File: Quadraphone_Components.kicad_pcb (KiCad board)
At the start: 4 copper layers, 60 x 100 mm, 196 parts, among them J1 Conn_01x10_Male, J2 Conn_01x10_Male, J3 Conn_01x10_Male, J4 Conn_01x10_Male, J5 Eurorack_10_pin_power, Q1 MMBT3904, U1 AMS1117-5.0, U10 TL072, U11 74LV4066PW, U12 SSI2131, U13 TL072, U14 LM4040DBZ-2.5, U15 74LV4066PW, U16 TL072, U17 SSI2131, U18 TL072, U22 SSI2131, U3 MCP6002, U4 LM4040DBZ-5, U5 MCP6004, U6 74LV4066PW, U7 74LV4066PW, U8 74LV4066PW, U9 SSI2131

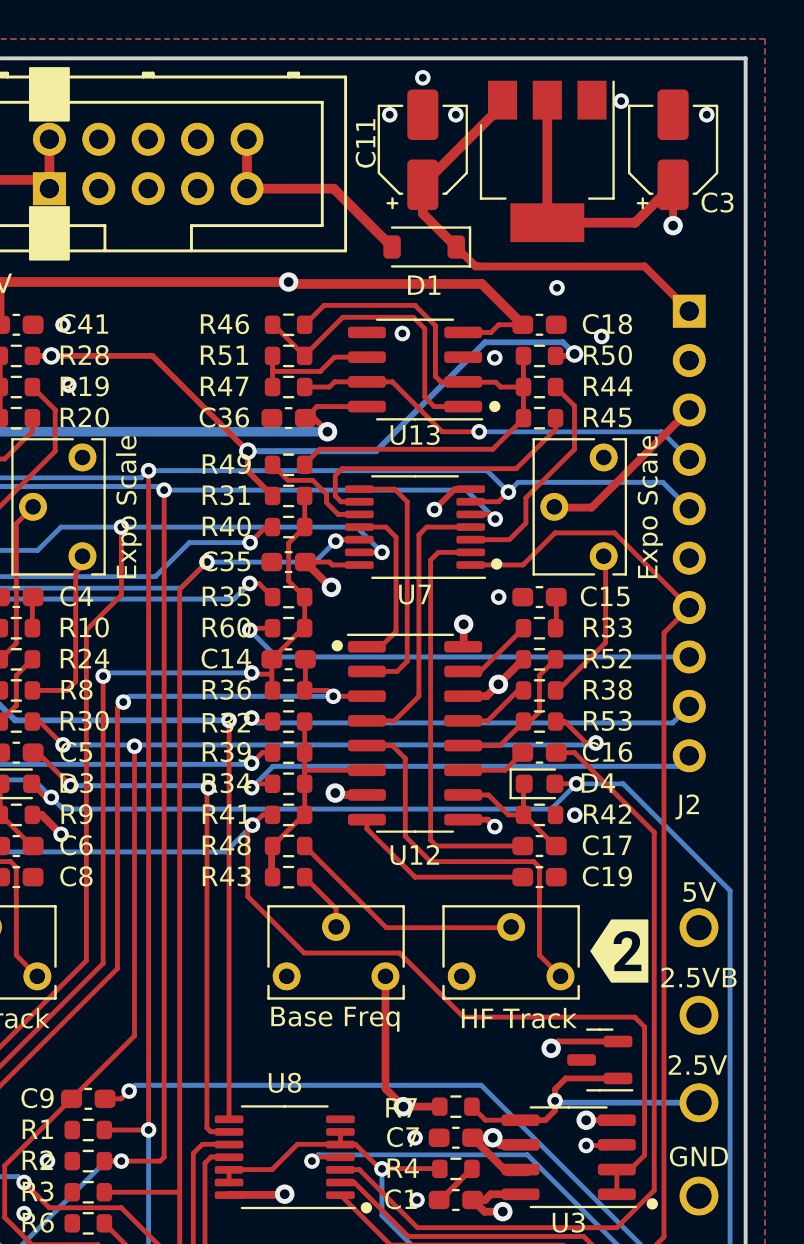
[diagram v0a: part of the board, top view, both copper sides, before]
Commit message: Updated resistor values in VCO tuning circuits
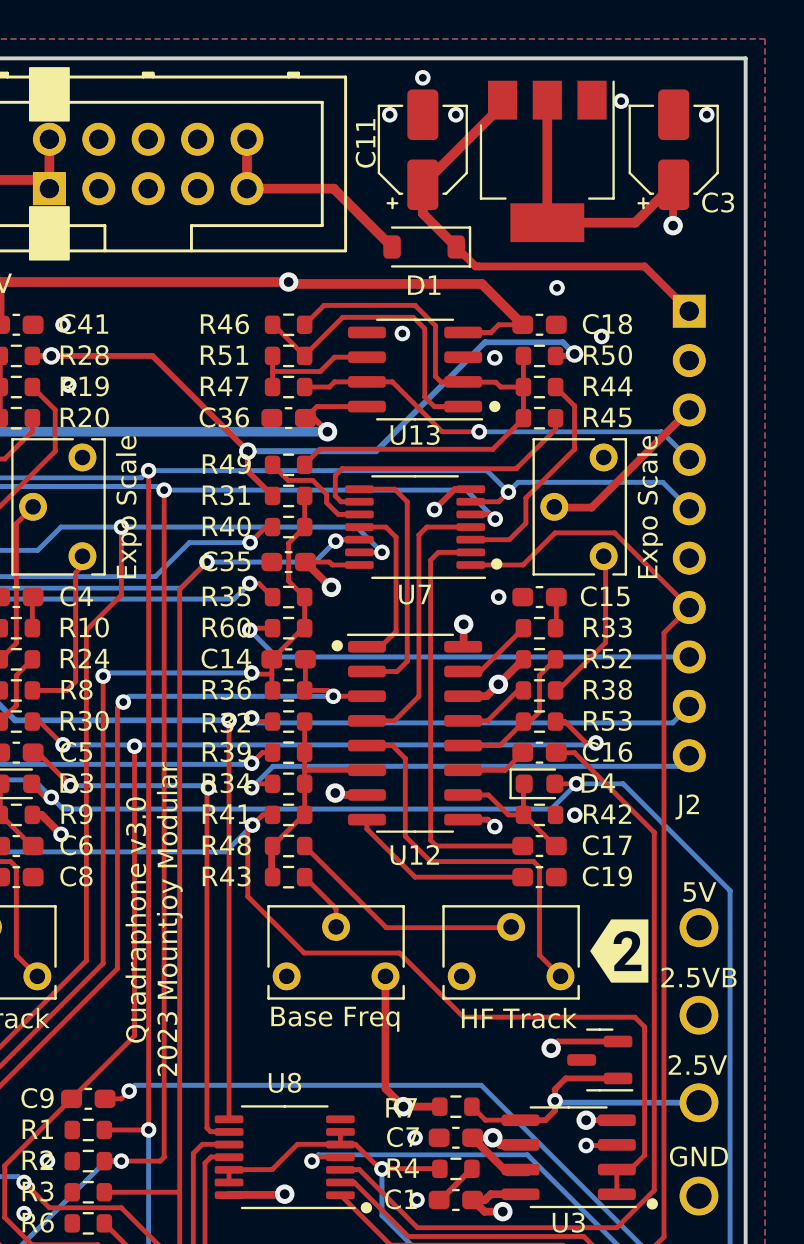
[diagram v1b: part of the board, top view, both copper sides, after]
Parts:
- R10, R16, R33, R48, R56, R71, R79, R94: value 267 -> 270
- R22, R41, R64, R87: value 68k -> 49.9k
- R23, R43, R66, R89: value 100k -> 68k
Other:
- board text added: "Quadraphone v3.0 2023 Mountjoy Modular"
- board text removed: "Quadraphone Components v3.0 Mountjoy Modular"
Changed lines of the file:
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@@
     (descr "Diode SMD 0603 (1608 Metric), square (rectangular) end terminal, IPC_7351 nominal, (Body size source: http://www.tortai-tech.com/upload/download/2011102023233369053.pdf), generated with kicad-footprint-generator")
     (tags "diode")
-    (property "Part_Number" "C8598")
+    (property "Part_Number" "")
     (property "Sheetfile" "OSCVoice.kicad_sch")
     (property "Sheetname" "OSCVoice1")
@@
         (effects (font (size 1 1) (thickness 0.15)))
     )
-    (fp_text value "100k" (at 0 1.43) (layer "F.Fab")
+    (fp_text value "68k" (at 0 1.43) (layer "F.Fab")
         (effects (font (size 1 1) (thickness 0.15)))
     )
@@
         (effects (font (size 1 1) (thickness 0.15)))
     )
-    (fp_text value "68k" (at 0 1.43) (layer "F.Fab")
+    (fp_text value "49.9k" (at 0 1.43) (layer "F.Fab")
         (effects (font (size 1 1) (thickness 0.15)))
     )
@@
         (effects (font (size 1 1) (thickness 0.15)))
     )
-    (fp_text value "68k" (at 0 1.43) (layer "F.Fab")
+    (fp_text value "49.9k" (at 0 1.43) (layer "F.Fab")
         (effects (font (size 1 1) (thickness 0.15)))
     )
@@
     (descr "Diode SMD 0603 (1608 Metric), square (rectangular) end terminal, IPC_7351 nominal, (Body size source: http://www.tortai-tech.com/upload/download/2011102023233369053.pdf), generated with kicad-footprint-generator")
     (tags "diode")
-    (property "Part_Number" "C8598")
+    (property "Part_Number" "")
     (property "Sheetfile" "OSCVoice.kicad_sch")
     (property "Sheetname" "OSCVoice4")
@@
     (descr "SMD capacitor, aluminum electrolytic, Panasonic, 4.0x5.8mm")
     (tags "capacitor electrolytic")
-    (property "Part_Number" "C134798")
-    (property "Rotation" "360")
     (property "Sheetfile" "Quadraphone_Components.kicad_sch")
     (property "Sheetname" "")
@@
         (effects (font (size 1 1) (thickness 0.15)))
     )
-    (fp_text value "267" (at 0 1.43) (layer "F.Fab")
+    (fp_text value "270" (at 0 1.43) (layer "F.Fab")
         (effects (font (size 1 1) (thickness 0.15)))
     )
@@
         (effects (font (size 1 1) (thickness 0.15)))
     )
-    (fp_text value "100k" (at 0 1.43) (layer "F.Fab")
+    (fp_text value "68k" (at 0 1.43) (layer "F.Fab")
         (effects (font (size 1 1) (thickness 0.15)))
     )
@@
         (effects (font (size 1 1) (thickness 0.15)))
     )
-    (fp_text value "100k" (at 0 1.43) (layer "F.Fab")
+    (fp_text value "68k" (at 0 1.43) (layer "F.Fab")
         (effects (font (size 1 1) (thickness 0.15)))
     )
@@
     (descr "SMD capacitor, aluminum electrolytic, Panasonic, 4.0x5.8mm")
     (tags "capacitor electrolytic")
-    (property "Part_Number" "C134793")
-    (property "Rotation" "270")
     (property "Sheetfile" "Quadraphone_Components.kicad_sch")
     (property "Sheetname" "")
@@
         (effects (font (size 1 1) (thickness 0.15)))
     )
-    (fp_text value "68k" (at 0 1.43) (layer "F.Fab")
+    (fp_text value "49.9k" (at 0 1.43) (layer "F.Fab")
         (effects (font (size 1 1) (thickness 0.15)))
     )
@@
         (effects (font (size 1 1) (thickness 0.15)))
     )
-    (fp_text value "100k" (at 0 1.43) (layer "F.Fab")
+    (fp_text value "68k" (at 0 1.43) (layer "F.Fab")
         (effects (font (size 1 1) (thickness 0.15)))
     )
@@
     (descr "SOD-123")
     (tags "SOD-123")
-    (property "Part_Number" "C8598")
     (property "Sheetfile" "Quadraphone_Components.kicad_sch")
     (property "Sheetname" "")
@@
     (descr "Diode SMD 0603 (1608 Metric), square (rectangular) end terminal, IPC_7351 nominal, (Body size source: http://www.tortai-tech.com/upload/download/2011102023233369053.pdf), generated with kicad-footprint-generator")
     (tags "diode")
-    (property "Part_Number" "C8598")
+    (property "Part_Number" "")
     (property "Sheetfile" "OSCVoice.kicad_sch")
     (property "Sheetname" "OSCVoice2")
@@
         (effects (font (size 1 1) (thickness 0.15)))
     )
-    (fp_text value "267" (at 0 1.43) (layer "F.Fab")
+    (fp_text value "270" (at 0 1.43) (layer "F.Fab")
         (effects (font (size 1 1) (thickness 0.15)))
     )
@@
         (effects (font (size 1 1) (thickness 0.15)))
     )
-    (fp_text value "267" (at 0 1.43) (layer "F.Fab")
+    (fp_text value "270" (at 0 1.43) (layer "F.Fab")
         (effects (font (size 1 1) (thickness 0.15)))
     )
@@
     (descr "Diode SMD 0603 (1608 Metric), square (rectangular) end terminal, IPC_7351 nominal, (Body size source: http://www.tortai-tech.com/upload/download/2011102023233369053.pdf), generated with kicad-footprint-generator")
     (tags "diode")
-    (property "Part_Number" "C8598")
+    (property "Part_Number" "")
     (property "Sheetfile" "OSCVoice.kicad_sch")
     (property "Sheetname" "OSCVoice3")
@@
         (effects (font (size 1 1) (thickness 0.15)))
     )
-    (fp_text value "267" (at 0 1.43) (layer "F.Fab")
+    (fp_text value "270" (at 0 1.43) (layer "F.Fab")
         (effects (font (size 1 1) (thickness 0.15)))
     )
@@
     (descr "SOD-123")
     (tags "SOD-123")
-    (property "Part_Number" "C8598")
     (property "Sheetfile" "Quadraphone_Components.kicad_sch")
     (property "Sheetname" "")
@@
         (effects (font (size 1 1) (thickness 0.15)))
     )
-    (fp_text value "267" (at 0 1.43) (layer "F.Fab")
+    (fp_text value "270" (at 0 1.43) (layer "F.Fab")
         (effects (font (size 1 1) (thickness 0.15)))
     )
@@
         (effects (font (size 1 1) (thickness 0.15)))
     )
-    (fp_text value "68k" (at 0 1.43) (layer "F.Fab")
+    (fp_text value "49.9k" (at 0 1.43) (layer "F.Fab")
         (effects (font (size 1 1) (thickness 0.15)))
     )
@@
         (effects (font (size 1 1) (thickness 0.15)))
     )
-    (fp_text value "267" (at 0 1.43) (layer "F.Fab")
+    (fp_text value "270" (at 0 1.43) (layer "F.Fab")
         (effects (font (size 1 1) (thickness 0.15)))
     )
@@
         (effects (font (size 1 1) (thickness 0.15)))
     )
-    (fp_text value "267" (at 0 1.43) (layer "F.Fab")
+    (fp_text value "270" (at 0 1.43) (layer "F.Fab")
         (effects (font (size 1 1) (thickness 0.15)))
     )
@@
   )
   (footprint "Capacitor_SMD:CP_Elec_4x5.7" (layer "F.Cu")
-    (at 106.26875 54.7 90)
+    (at 106.3 54.7 90)
     (descr "SMD capacitor, aluminum electrolytic, United Chemi-Con, 4.0x5.7mm")
     (tags "capacitor electrolytic")
@@
         (effects (font (size 1 1) (thickness 0.15)))
     )
-    (fp_text value "267" (at 0 1.43) (layer "F.Fab")
+    (fp_text value "270" (at 0 1.43) (layer "F.Fab")
         (effects (font (size 1 1) (thickness 0.15)))
     )
@@
     (property "Sheetfile" "Quadraphone_Components.kicad_sch")
     (property "Sheetname" "")
+    (property "exclude_from_bom" "")
     (property "ki_description" "Generic connector, single row, 01x10, script generated (kicad-library-utils/schlib/autogen/connector/)")
     (property "ki_keywords" "connector")
@@
     (property "Sheetfile" "Quadraphone_Components.kicad_sch")
     (property "Sheetname" "")
+    (property "exclude_from_bom" "")
     (property "ki_description" "Generic connector, single row, 01x10, script generated (kicad-library-utils/schlib/autogen/connector/)")
     (property "ki_keywords" "connector")
@@
     (property "Sheetfile" "Quadraphone_Components.kicad_sch")
     (property "Sheetname" "")
+    (property "exclude_from_bom" "")
     (property "ki_description" "Generic connector, single row, 01x10, script generated (kicad-library-utils/schlib/autogen/connector/)")
     (property "ki_keywords" "connector")
@@
     (property "Sheetfile" "Quadraphone_Components.kicad_sch")
     (property "Sheetname" "")
+    (property "exclude_from_bom" "")
     (property "ki_description" "Generic connector, single row, 01x10, script generated (kicad-library-utils/schlib/autogen/connector/)")
     (property "ki_keywords" "connector")
@@
   (gr_line locked (start 50 150) (end 110 150)
     (stroke (width 0.2) (type solid)) (layer "Edge.Cuts"))
-  (gr_text "Quadraphone Components v3.0\nMountjoy Modular" (at 80 63) (layer "B.SilkS")
-    (effects (font (size 1 1) (thickness 0.15)) (justify mirror))
-  )
   (gr_text "2.5VB" (at 107.6 97.3) (layer "F.SilkS")
     (effects (font (size 1 1) (thickness 0.15)))
@@
     (effects (font (size 1 1) (thickness 0.15)))
   )
+  (gr_text "Quadraphone v3.0\n2023 Mountjoy Modular" (at 79.5 94.3 90) (layer "F.SilkS")
+    (effects (font (size 1 1) (thickness 0.15)))
+  )
